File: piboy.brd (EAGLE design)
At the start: 76.2 x 76.2 mm, 69 parts, among them CN4 MicroUSB, T1 MMUN2133LT1G, U1 TPS61090RSAR, U2 MCP73871, U3 TPA2005D1

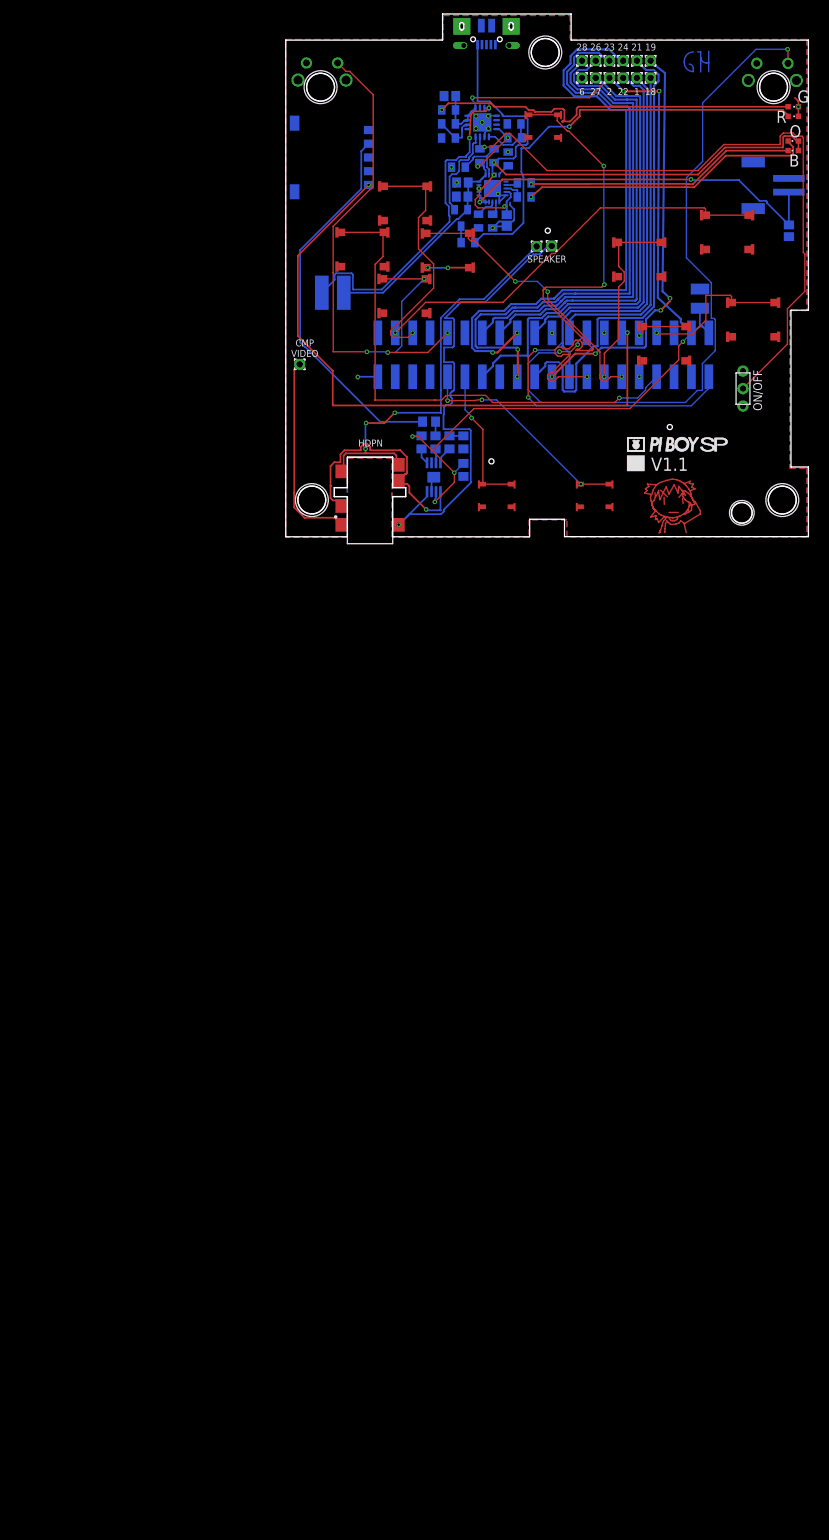
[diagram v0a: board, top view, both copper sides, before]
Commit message: -finished the PAM8302A audio amp
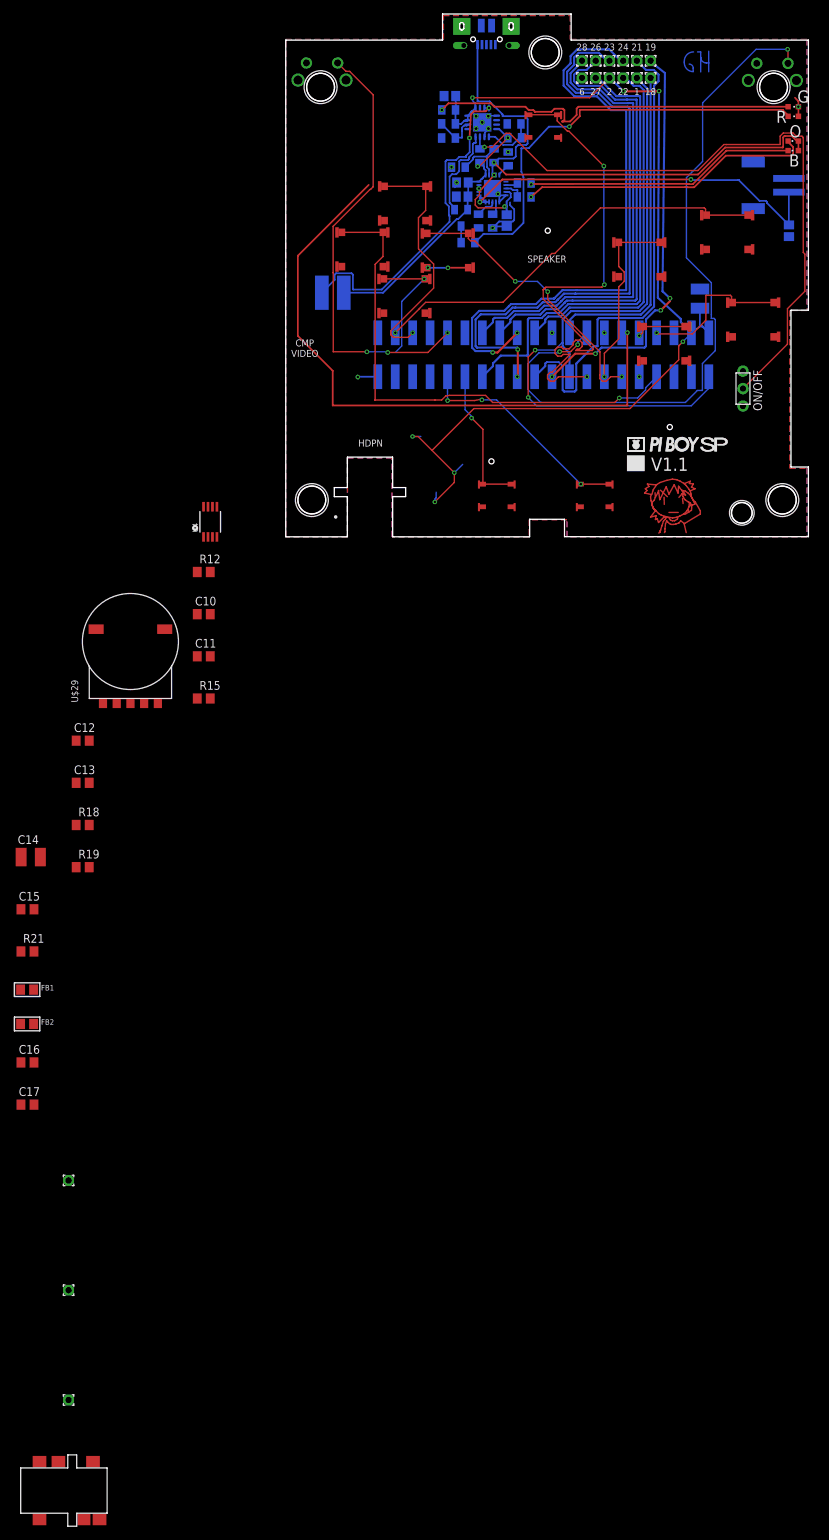
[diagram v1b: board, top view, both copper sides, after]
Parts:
- removed C3, C5: 1uF, resistor:C0805
- removed C9: 10uF, resistor:C0805
- removed CMP_VIDEO_OUT, SPK1, SPK2: (no value), piboy_new:WIREPAD_1,6/0,9
- removed R10, R11: 150K, resistor:R0805
- removed R9: 10K, resistor:R0805
- removed U$33: RK10J12R0A0B, piboy_new:RK10J12R0A0B
- removed U$40: SJ-43504-SMT-TR, SJ-43504-SMT-TR:SJ-43504-SMT-TR
- removed U3: TPA2005D1, SparkFun-IC-Amplifiers:POWER-SOP8
- added C10: 33nF, resistor:C0805
- added C11: 10uF, resistor:C0805
- added C12, C13: 1uF, resistor:C0805
- added C14: 100uF, resistor:C1210
- added C15: 100nF, resistor:C0805
- added C16, C17: 22pF, resistor:C0805
- added CMP_VIDEO_OUT1, SPK3, SPK4: (no value), piboy_new:WIREPAD_1,6/0,9
- added FB1, FB2: (no value), Adafruit PAM8302:0805
- added R12: 270, resistor:R0805
- added R15: 150, resistor:R0805
- added R18, R19: 100, resistor:R0805
- added R21: 10k, resistor:R0805
- added U$29: RK10J12R0A0B, piboy_new:RK10J12R0A0B
- added U$30: SJ-43504-SMT-TR, SJ-43504-SMT-TR:SJ-43504-SMT-TR
- added U4: (no value), Adafruit PAM8302:MSOP8_0.65MM
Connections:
- net 3.3V renamed +3.3V
- removed net 5.0V: BCM2,5.0V.1, C2.1, C6.1, C9.2, R3.2, R5.1, R9.1, U$9.P2, U$9.P4, U1.1, U1.15, U1.16, U3.6
- removed net CMP_VIDEO_OUT: CMP_VIDEO_OUT.1, U$40.P$1
- removed net N$17: R9.2, U3.1
- removed net N$20: C5.1, R10.2
- removed net N$21: C3.1, R11.2
- removed net N$22: R10.1, U$33.P$2
- removed net N$23: C5.2, U3.3
- removed net N$26: C3.2, U3.4
- new net +5V: BCM2,5.0V.1, C14.1, C15.1, C2.1, C6.1, R21.2, R3.2, R5.1, U$9.P2, U$9.P4, U1.1, U1.15, U1.16, U4.6
- new net CMP_VIDEO_OUT1: CMP_VIDEO_OUT1.1, U$30.P$1
- new net N$18: C10.1, C11.1, R12.2
- new net N$35: C11.2, R15.2, U$29.P$3
- new net N$37: C12.1, U$29.P$2
- new net N$38: C13.1, U$29.GND1, U$29.GND2, U$29.P$1
- new net N$39: C13.2, R19.2
- new net N$40: C12.2, R18.2
- new net N$41: R18.1, U4.3
- new net N$42: R19.1, U4.4
- new net N$45: R21.1, U4.1
- new net N$47: FB1.1, U4.8
- new net N$48: FB2.1, U4.5
- net AUD+: now also C17.1, FB2.2, U$30.P$2, U$30.P$3\; no longer U$40.P$2, U$40.P$3\, U3.5
- net AUD+_HDPN_OUT: now also SPK4.1, U$30.P$5, U$30.P$6; no longer SPK2.1, U$40.P$5, U$40.P$6
- net AUD-: now also C16.1, FB1.2, SPK3.1, U$30.P$4; no longer SPK1.1, U$40.P$4, U3.8
- net GND: now also C10.2, C14.2, C15.2, C16.2, C17.2, R15.1, U4.7; no longer C9.1, R11.1, U$33.GND1, U$33.GND2, U$33.P$1, U3.7, U3.9
- net PWM0: now also R12.1; no longer U$33.P$3
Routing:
- net 5.0V: track 147.3 -> 0.00 mm, vias 7 -> 0
- net +5V: track 0.00 -> 146.9 mm, vias 0 -> 7
- net AUD-: track 72.9 -> 0.00 mm, vias 1 -> 0
- net AUD+_HDPN_OUT: track 60.7 -> 0.00 mm, vias 3 -> 0
- net N$22: track 55.7 -> 0.00 mm
- net AUD+: track 37.3 -> 0.00 mm, vias 1 -> 0
- net CMP_VIDEO_OUT: track 29.1 -> 0.00 mm
- net N$26: track 2.57 -> 0.00 mm
- net N$17: track 2.36 -> 0.00 mm
- net GND: track 31.7 -> 29.4 mm
- net N$20: track 2.07 -> 0.00 mm
- net N$23: track 2.06 -> 0.00 mm
- net N$21: track 2.03 -> 0.00 mm
- net PWM0: vias 2 -> 1

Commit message: -did some wiring
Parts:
- C1, C7: device adafruit:C0805 -> resistor:C1210
- C6: device adafruit:C1210 -> resistor:C1210
- moved SPK4 179.2 mm to (40.1, 38.4)
- moved SPK3 163.1 mm to (36.5, 38.4)
- moved U$30 151.3 mm to (15.5, -1.07), turned to 90 degrees
- moved CMP_VIDEO_OUT1 123.7 mm to (2.65, 25.0)
- moved C17 109.3 mm to (20.9, 9.54), flipped to the bottom, turned to 270 degrees
- moved FB2 101.7 mm to (20.0, 12.8), flipped to the bottom
- moved R21 101.4 mm to (30.7, 14.5), flipped to the bottom, turned to 180 degrees
- moved C15 100.0 mm to (34.9, 14.5), flipped to the bottom, turned to 180 degrees
- moved C16 99.1 mm to (19.9, 4.03), flipped to the bottom, turned to 180 degrees
- moved FB1 88.9 mm to (19.9, 1.69), flipped to the bottom
- moved C14 83.3 mm to (25.2, 8.56), flipped to the bottom, turned to 270 degrees
- moved R19 83.1 mm to (29.4, 10.3), flipped to the bottom, turned to 180 degrees
- moved R18 81.2 mm to (30.7, 12.4), flipped to the bottom, turned to 180 degrees
- moved R15 79.7 mm to (15.2, 51.3), flipped to the bottom
- moved C12 76.9 mm to (34.8, 12.4), flipped to the bottom
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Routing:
- net +5V: track 146.9 -> 20.6 mm, vias 7 -> 0
- net J_RSH: track 104.7 -> 0.00 mm, vias 3 -> 0
- net +3.3V: track 96.9 -> 0.00 mm, vias 2 -> 0
- net ENABLE: track 95.8 -> 1.77 mm, vias 1 -> 0
- net PWM0: track 93.0 -> 0.00 mm, vias 1 -> 0
- net TFT_CS: track 86.9 -> 0.00 mm, vias 2 -> 0
- net SCLK: track 86.2 -> 0.00 mm, vias 2 -> 0
- net J_BRT: track 76.8 -> 0.00 mm, vias 3 -> 0
- net J_LFT: track 74.5 -> 0.00 mm, vias 1 -> 0
- net MISO: track 70.1 -> 0.00 mm
- net EEDATA: track 68.3 -> 0.00 mm
- net EECLK: track 66.9 -> 0.00 mm
- net RT_CS: track 66.5 -> 0.00 mm
- net J_LSH: track 64.9 -> 0.00 mm, vias 3 -> 0
- net VBUS: track 95.9 -> 33.3 mm
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
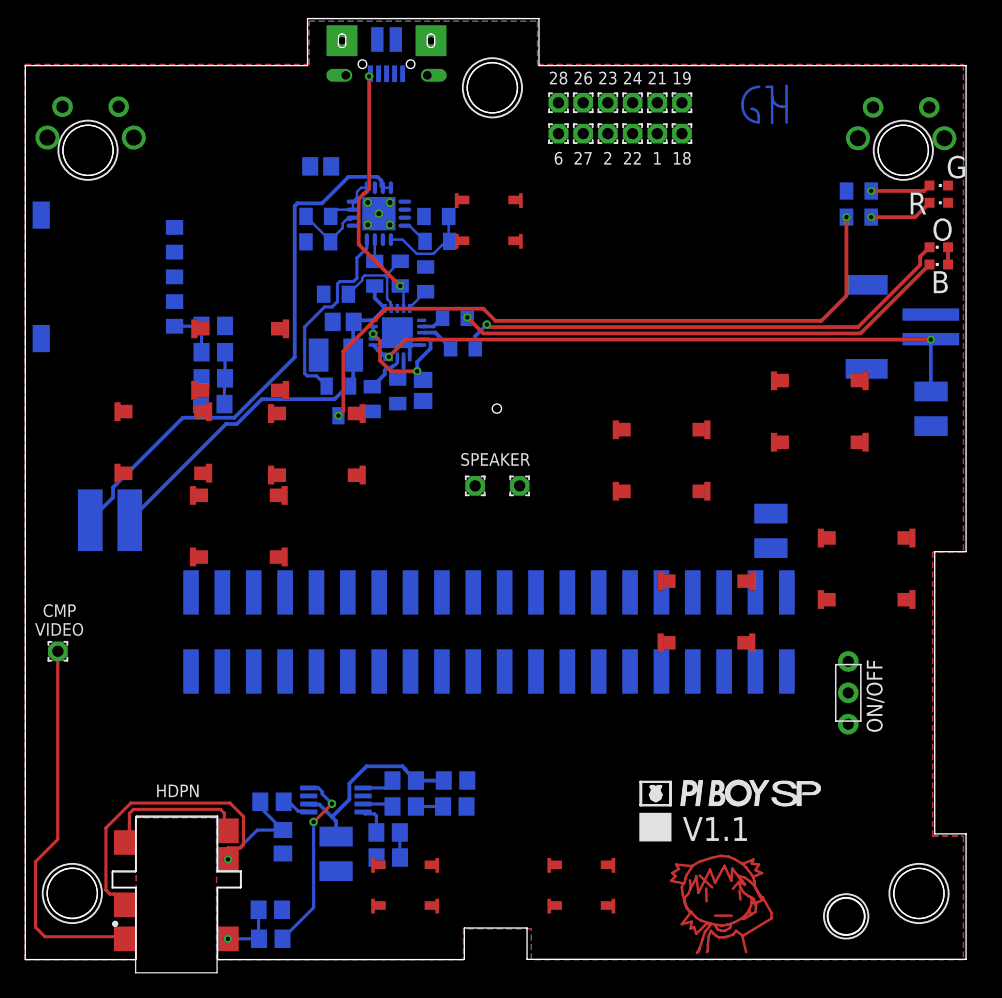
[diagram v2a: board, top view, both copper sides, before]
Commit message: -performed a DRC, no errors TODO fix silkscreen layers clean up wires
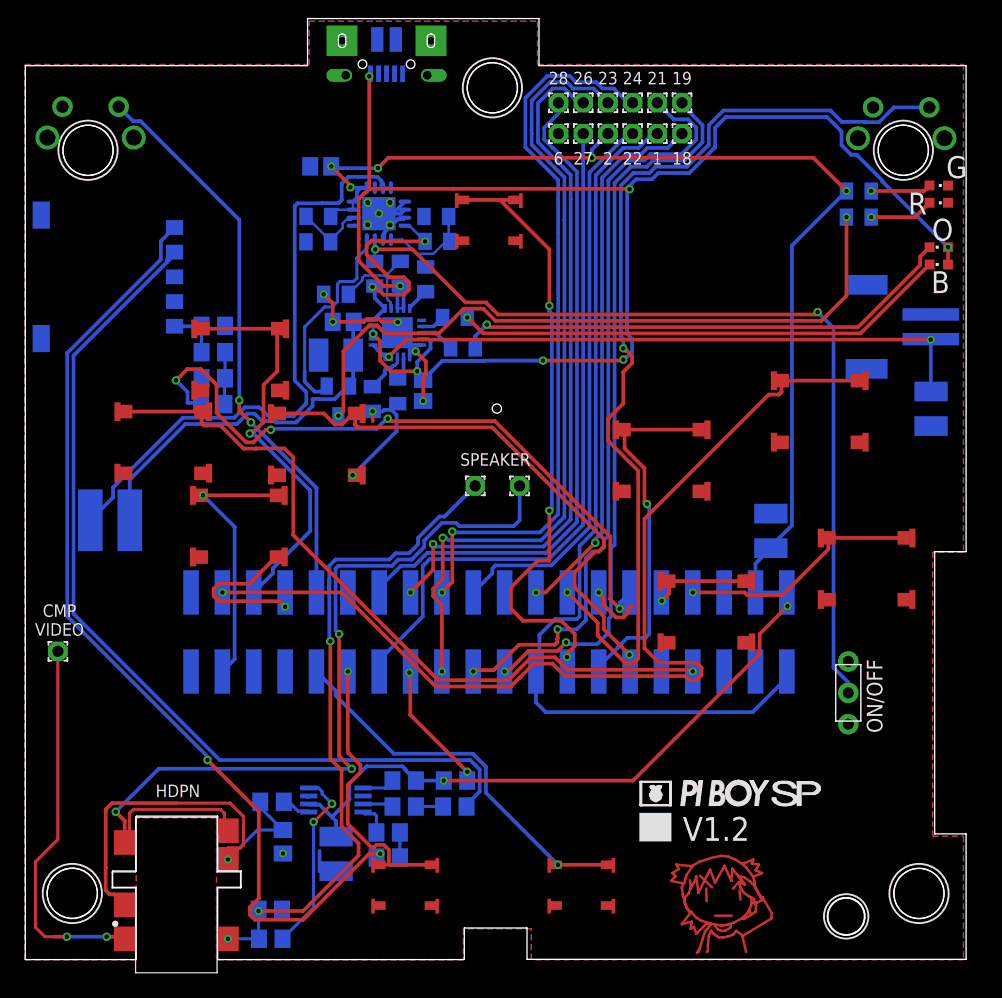
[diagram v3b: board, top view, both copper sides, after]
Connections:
- net N$38: no longer U$29.GND1, U$29.GND2
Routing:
- net +5V: track 20.6 -> 144.0 mm, vias 0 -> 7
- net VBUS: track 33.3 -> 125.0 mm, vias 4 -> 8
- net J_X: track 0.00 -> 82.1 mm, vias 0 -> 1
- net N$38: track 0.00 -> 79.4 mm, vias 0 -> 2
- net J_RSH: track 0.00 -> 78.7 mm, vias 0 -> 2
- net +3.3V: track 0.00 -> 76.0 mm
- net N$37: track 0.00 -> 75.1 mm
- net ENABLE: track 1.77 -> 72.2 mm, vias 0 -> 2
- net SCLK: track 0.00 -> 64.5 mm, vias 0 -> 2
- net GND: track 4.69 -> 67.1 mm, vias 0 -> 12
- net MISO: track 0.00 -> 61.5 mm, vias 0 -> 2
- net J_LFT: track 0.00 -> 60.3 mm, vias 0 -> 1
- net AUD+_HDPN_OUT: track 12.6 -> 72.5 mm, vias 0 -> 3
- net TFT_CS: track 0.00 -> 59.6 mm, vias 0 -> 2
- net MOSI: track 0.00 -> 58.8 mm, vias 0 -> 2
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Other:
- board text added: "V1.2"
- board text removed: "V1.1"

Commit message: -added license info on the schematic
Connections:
- net N$18: now also R15.2
- net N$35: no longer R15.2
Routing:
- net N$34: track 59.3 -> 0.00 mm
- net N$21: track 0.00 -> 8.67 mm
- net N$23: track 0.00 -> 8.67 mm
- net J_X: track 82.1 -> 74.7 mm, vias 1 -> 3
- net GND: track 67.1 -> 59.7 mm
- net N$19: track 4.94 -> 1.12 mm
- net N$25: track 0.38 -> 3.95 mm
- net N$14: track 0.00 -> 3.20 mm
- net N$18: track 4.22 -> 7.14 mm
- net N$17: track 0.00 -> 2.01 mm
- net N$27: track 1.67 -> 0.00 mm
- net N$29: track 1.57 -> 0.00 mm
- net N$28: track 1.50 -> 0.00 mm
- net N$24: track 1.69 -> 0.20 mm
- net N$36: track 1.40 -> 0.00 mm
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
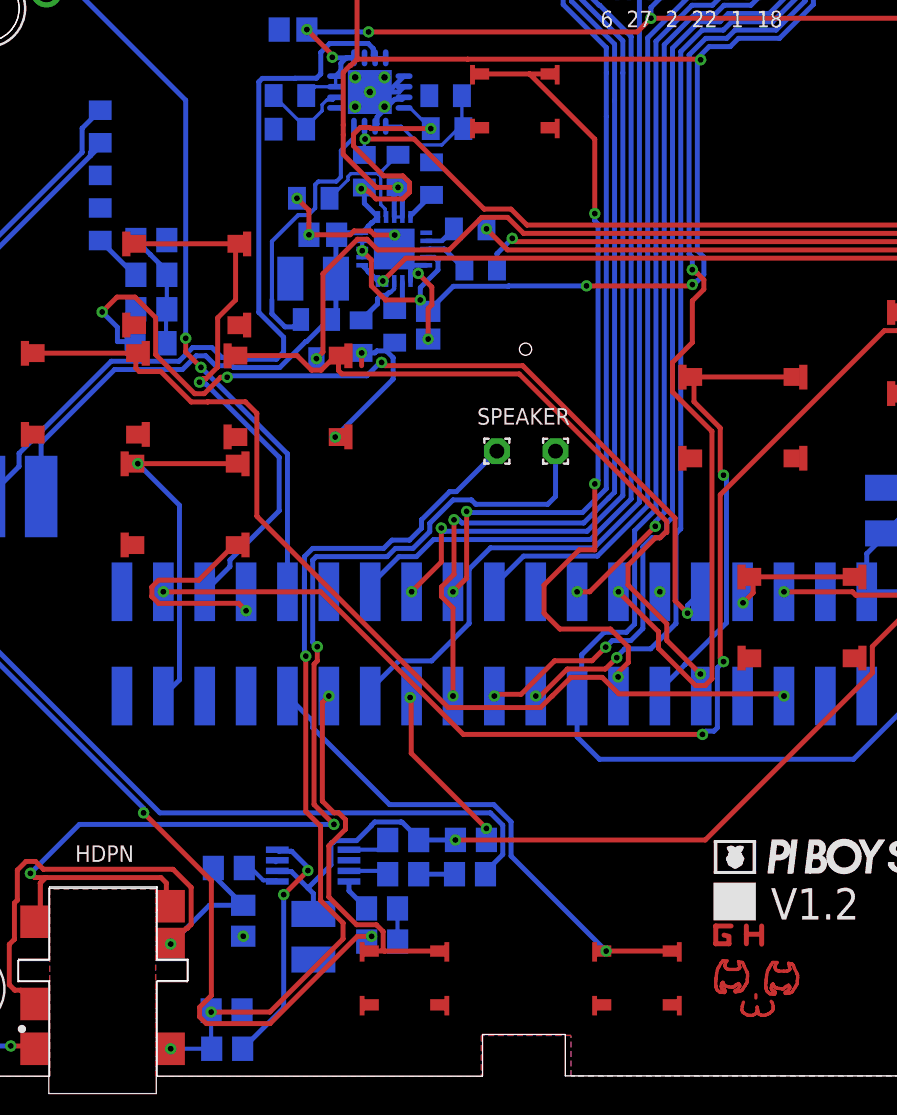
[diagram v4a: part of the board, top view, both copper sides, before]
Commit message: -corrected license info
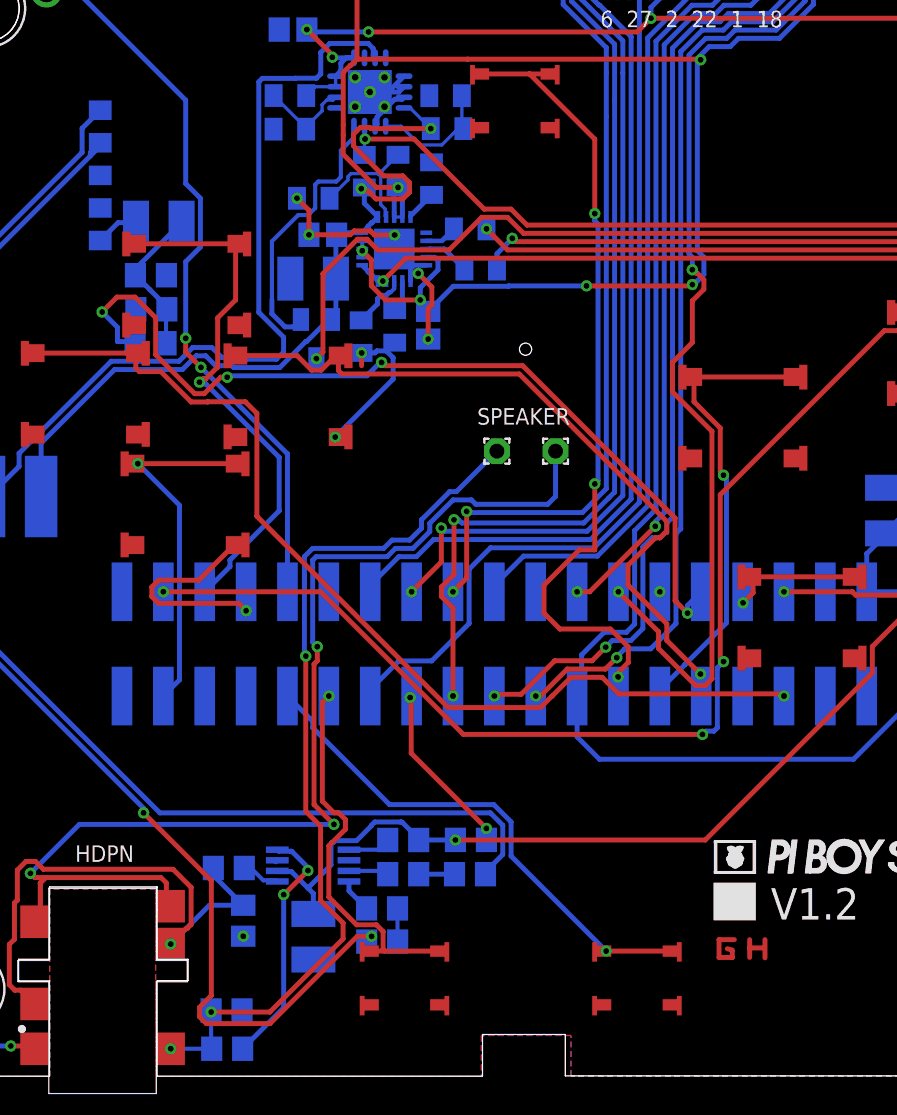
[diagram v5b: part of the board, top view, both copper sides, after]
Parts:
- C11: device resistor:C0805 -> resistor:C1210
- moved C11 3.23 mm to (15.7, 52.4)
- moved R15 2.16 mm to (15.2, 49.2)
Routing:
- net N$21: track 8.67 -> 0.00 mm
- net N$23: track 8.67 -> 0.00 mm
- net N$25: track 3.95 -> 0.00 mm
- net N$18: track 7.14 -> 9.39 mm
- net N$20: track 0.92 -> 0.00 mm
- net N$22: track 0.92 -> 0.00 mm
- net J_LSH: track 46.3 -> 47.1 mm
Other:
- board text added: "PiBoy SP by Grant Haack https://www.granthaack.com/piboy-sp PCB Layout and Design is licensed under Creative Commons Attribution-NonCommercial 4.0 International (CC BY-NC 4.0)"
